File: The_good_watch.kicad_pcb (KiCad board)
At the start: 2 copper layers, 45 x 45 mm, 42 parts, among them IC1 DW01A, J1 Main, J2 USB_B_Micro, J3 PROG, J4 Screen, J5 Button, J6 70AAJ-6-M0G, M1 Motor_DC, Q1 FS8205A, SW1 SW_Push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

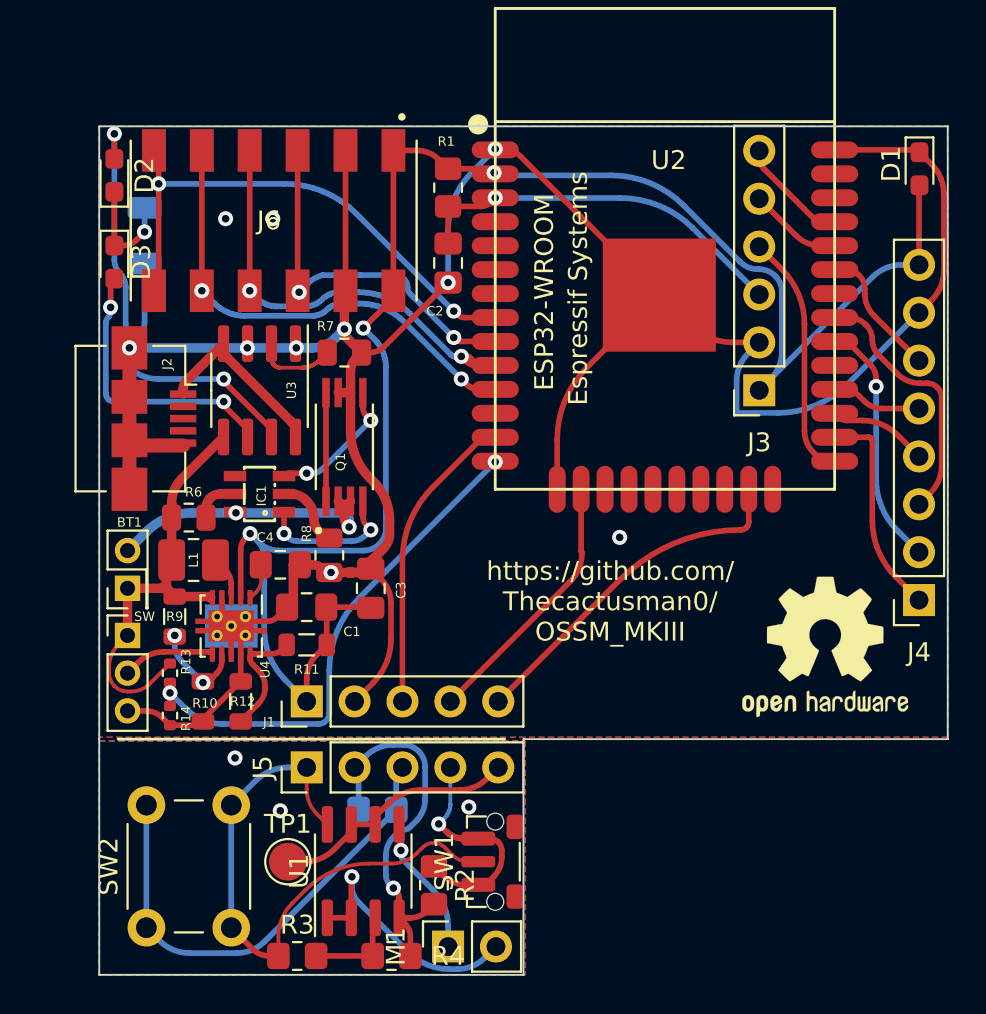
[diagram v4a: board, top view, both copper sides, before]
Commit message: Changed spring connector for modules to pinheaders.
still need to update modules
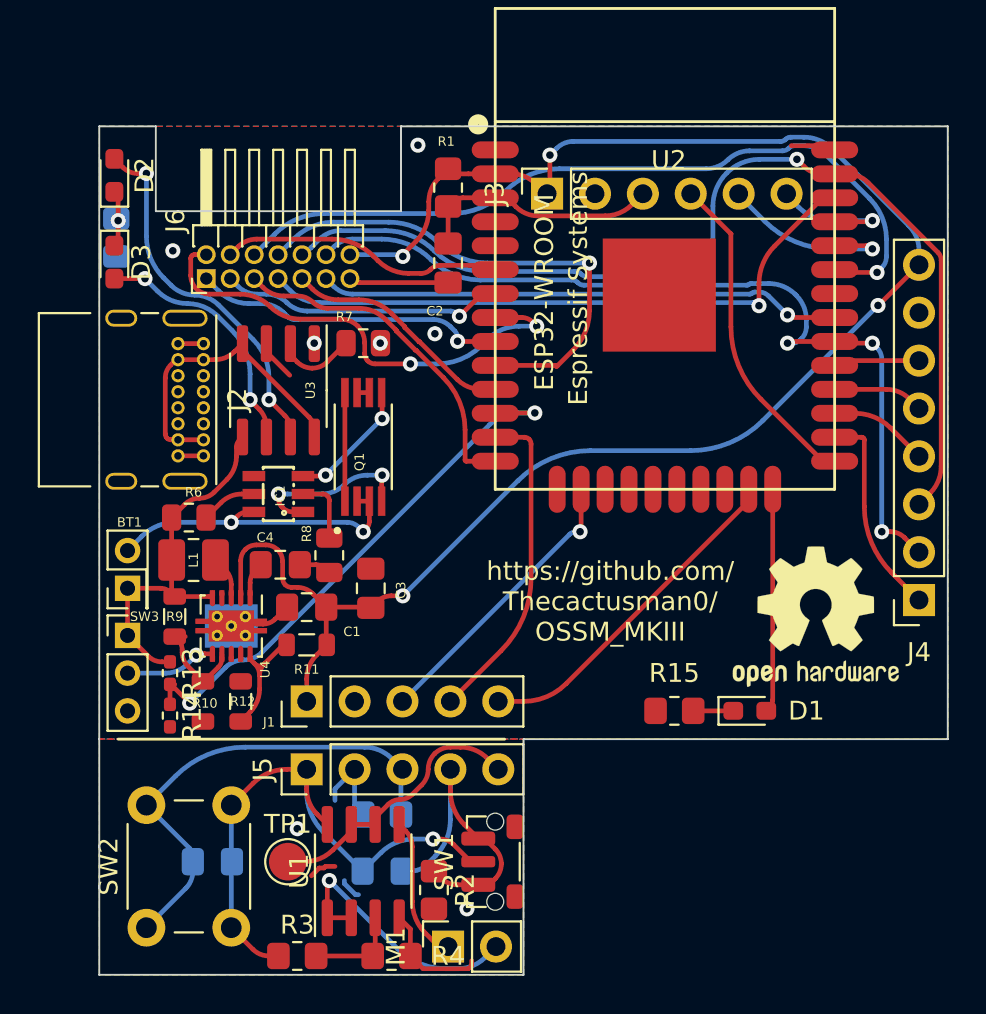
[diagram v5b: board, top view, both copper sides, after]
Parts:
- removed JP1: CHRG, Capacitor_SMD:C_1206_3216Metric
- added C5: 100nF, Capacitor_SMD:C_0805_2012Metric_Pad1.18x1.45mm_HandSolder, B.Cu at (115.0, 89.5)
- added C6: 100nF, Capacitor_SMD:C_0805_2012Metric_Pad1.18x1.45mm_HandSolder, B.Cu at (106.0, 89.0)
- added R15: 2K, Resistor_SMD:R_0805_2012Metric_Pad1.20x1.40mm_HandSolder, F.Cu at (130.5, 81.0)
- added R16: 2K, Resistor_SMD:R_0805_2012Metric_Pad1.20x1.40mm_HandSolder, B.Cu at (100.9, 55.9)
- C2: value 0.1uF -> 1uF
- J2: value USB_B_Micro -> USB_C_Receptacle_USB2.0; footprint Connector_USB:USB_Micro-B_Amphenol_10104110_Horizontal -> Connector_USB:USB_C_Receptacle_GCT_USB4085
- J6: value 70AAJ-6-M0G -> Conn_02x07_Counter_Clockwise; footprint 70AAJ-6-M0G:BOURNS_70AAJ-6-M0G -> Connector_PinHeader_1.27mm:PinHeader_2x07_P1.27mm_Horizontal
- R13, R14: footprint Resistor_SMD:R_0402_1005Metric -> Resistor_SMD:R_0402_1005Metric_Pad0.72x0.64mm_HandSolder
- moved D1 30.1 mm to (134.5, 81.0), turned to 0 degrees
- moved J3 15.3 mm to (123.8, 53.6), turned to 90 degrees
- moved J2 4.76 mm to (105.5, 61.5)
- moved J6 4.72 mm to (105.7, 58.1), turned to 90 degrees
- moved REF** 1.68 mm to (138.0, 76.0)
- moved R7 1.12 mm to (114.0, 61.5)
- moved IC1 1.00 mm to (109.5, 69.5)
- moved Q1 1.00 mm to (114.0, 67.0)
- moved U3 1.00 mm to (109.5, 64.0)
- moved R5 0.35 mm to (115.0, 86.5)
- moved R2 0.25 mm to (117.8, 90.5)
- moved J5 0.10 mm to (111.0, 84.1)
- renumbered SW to SW3
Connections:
- D1 pad 1: GND -> Net-(D1-Pad1)
- D1 pad 2: +3V3 -> IO2
- J6 pad 1: +3V3 -> SENSE
- J6 pad 10: SENSE -> MOSI
- J6 pad 11: GND -> MISO
- J6 pad 12: +3V3 -> SCK
- J6 pad 2: GND -> ANALOG0
- J6 pad 3: SENSE -> ANALOG1
- J6 pad 4: SDA -> ANALOG2
- J6 pad 5: SCL -> MGPIO0
- J6 pad 6: ANALOG -> MGPIO1
- J6 pad 7: ANALOG -> MGPIO2
- J6 pad 8: SCL -> SDA
- J6 pad 9: SDA -> SCL
- Q1 pad 1: Net-(Q1-Pad1) -> unconnected-(Q1-Pad1)
- Q1 pad 8: Net-(Q1-Pad1) -> unconnected-(Q1-Pad1)
- R13 pad 2: IO12 -> IO27
- R14 pad 1: IO12 -> IO27
- U2 pad 12: unconnected-(U2-Pad12) -> IO27
- U2 pad 13: B2_M -> B1_M
- U2 pad 14: IO12 -> MGPIO0
- U2 pad 16: B1_M -> B2_M
- U2 pad 24: unconnected-(U2-Pad24) -> IO2
- U2 pad 29: unconnected-(U2-Pad29) -> CS
- U2 pad 31: MOSI -> MISO
- U2 pad 33: CS -> MGPIO1
- U2 pad 36: MISO -> MGPIO2
- U2 pad 37: unconnected-(U2-Pad37) -> MOSI
- U2 pad 6: unconnected-(U2-Pad6) -> ANALOG2
- U2 pad 7: unconnected-(U2-Pad7) -> ANALOG1
- U2 pad 8: ANALOG -> ANALOG0
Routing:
- net GND: track 180.7 -> 27.6 mm, vias 14 -> 7
- net MGPIO1: track 0.00 -> 42.0 mm, vias 0 -> 1
- net MOSI: track 13.9 -> 55.2 mm, vias 0 -> 1
- net MGPIO2: track 0.00 -> 33.6 mm, vias 0 -> 1
- net SCK: track 13.1 -> 46.4 mm, vias 1 -> 3
- net IO27: track 0.00 -> 29.3 mm, vias 0 -> 2
- net ANALOG: track 28.2 -> 0.00 mm, vias 2 -> 0
- net MISO: track 0.00 -> 27.8 mm, vias 0 -> 1
- net IO12: track 27.2 -> 0.00 mm, vias 2 -> 0
- net ANALOG0: track 0.00 -> 27.1 mm, vias 0 -> 2
- net MGPIO0: track 0.00 -> 18.2 mm
- net ANALOG1: track 0.00 -> 15.1 mm, vias 0 -> 1
- net ANALOG2: track 0.00 -> 15.0 mm
- net SCL: track 25.3 -> 12.4 mm, vias 2 -> 0
- net IO2: track 0.00 -> 11.9 mm
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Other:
- outline, holes or cut-outs redrawn

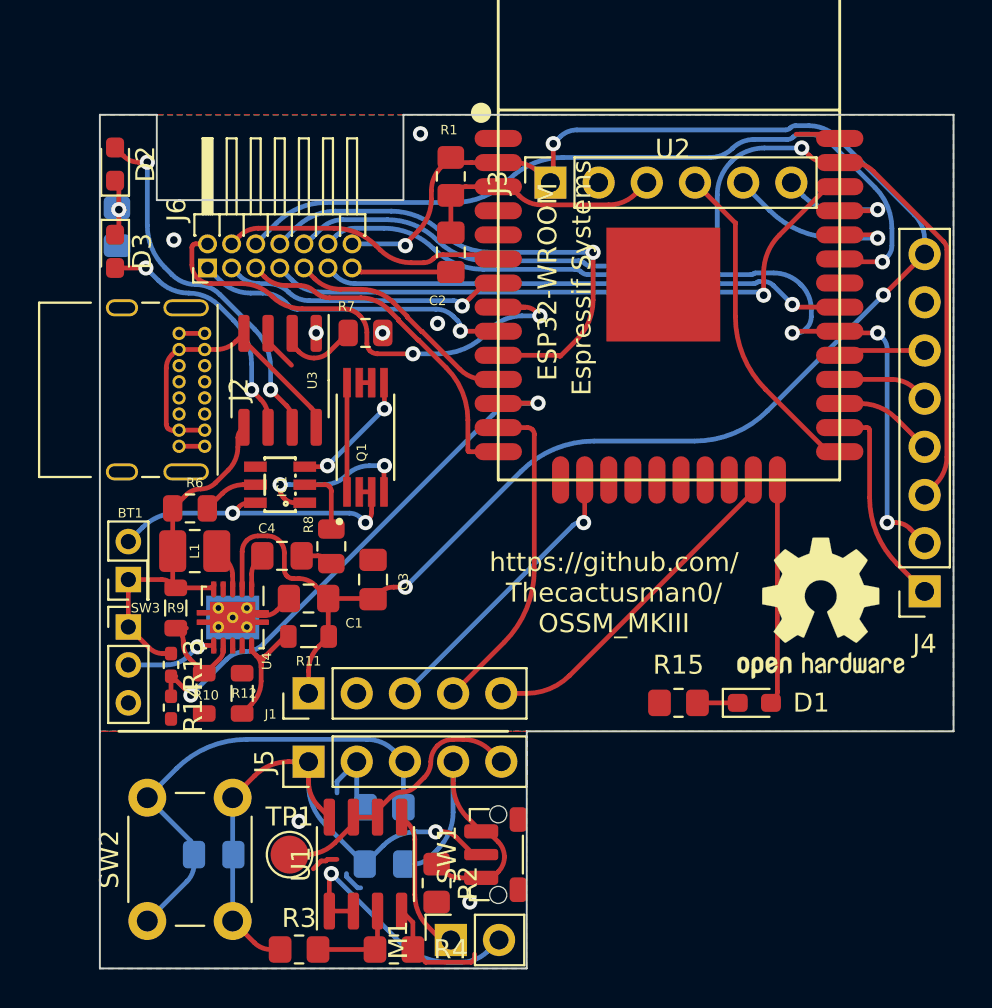
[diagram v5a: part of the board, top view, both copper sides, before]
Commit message: Graphical fixes, minor electrical fixes and enviro sensor module trial
Fixed some component values and added i2c pullups
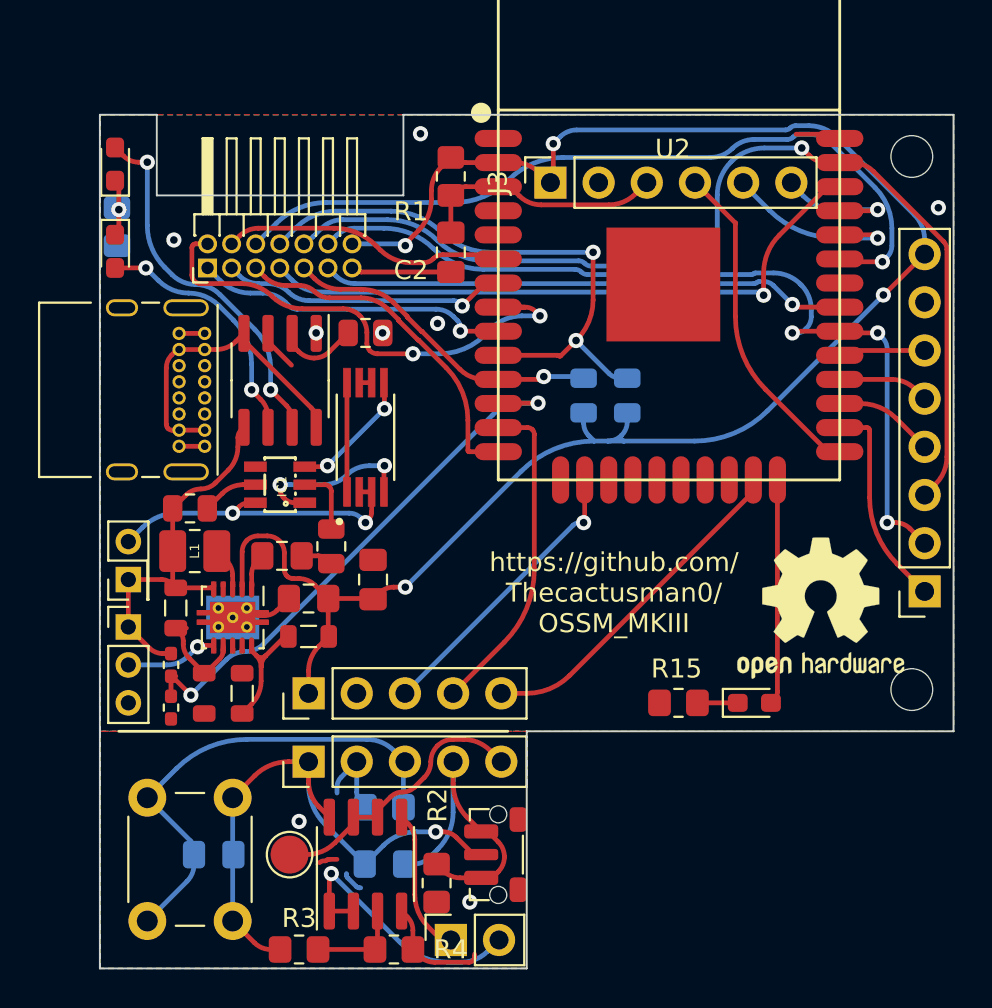
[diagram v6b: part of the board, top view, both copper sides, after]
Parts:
- added R17: 4.7K, Resistor_SMD:R_0805_2012Metric, B.Cu at (125.5, 64.8)
- added R18: 4.7K, Resistor_SMD:R_0805_2012Metric, B.Cu at (127.8, 64.8)
- added REF**: MountingHole_2.2mm_M2, MountingHole:MountingHole_2.2mm_M2, F.Cu at (142.8, 52.2)
- added REF**: MountingHole_2.2mm_M2, MountingHole:MountingHole_2.2mm_M2, F.Cu at (142.8, 80.3)
- renumbered Q1 to Qe, R8 to Re
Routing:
- net SCL: track 12.4 -> 17.0 mm, vias 0 -> 1
- net +3V3: track 123.2 -> 127.3 mm
- net SDA: track 27.0 -> 30.4 mm, vias 1 -> 2
- net (no net): track 2.61 -> 0.00 mm
- net GND: track 27.6 -> 29.4 mm, vias 7 -> 8
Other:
- outline, holes or cut-outs redrawn

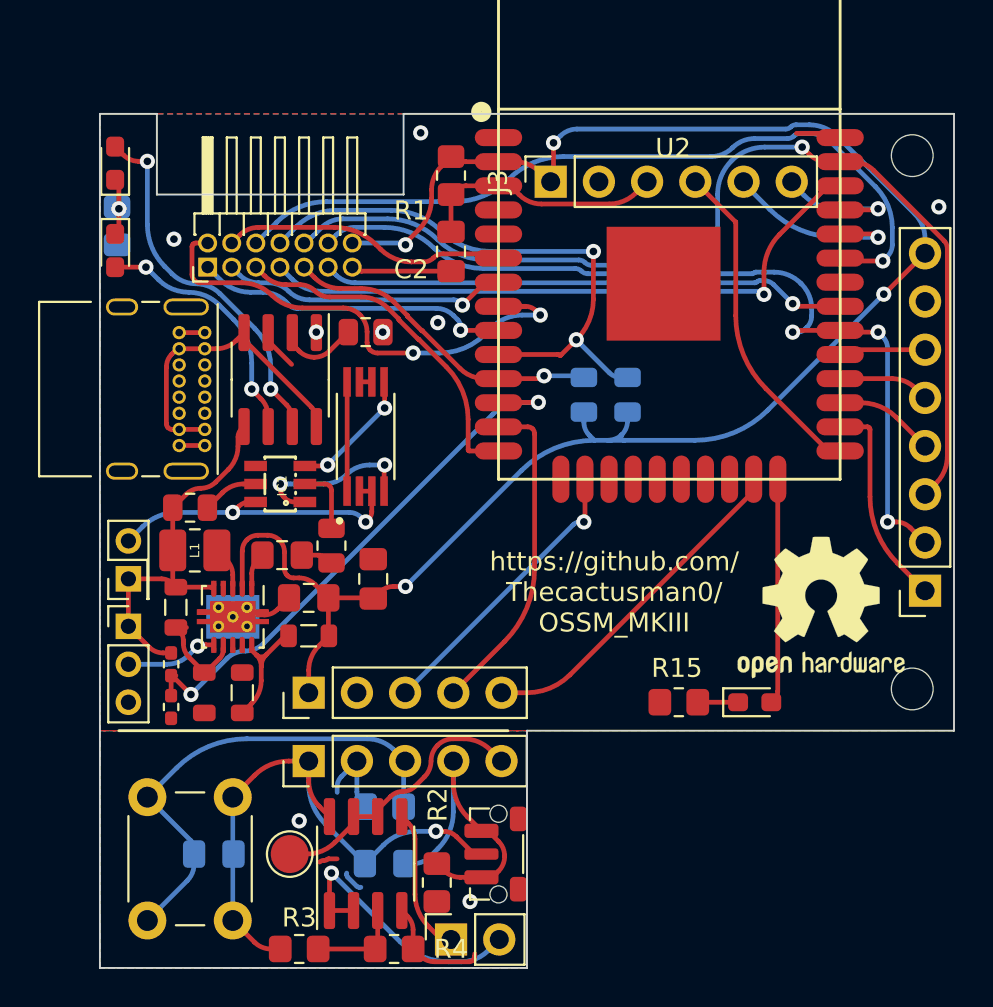
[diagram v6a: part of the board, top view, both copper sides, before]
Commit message: Added power switching
Uses usb power when plugged in and disconnects battery.
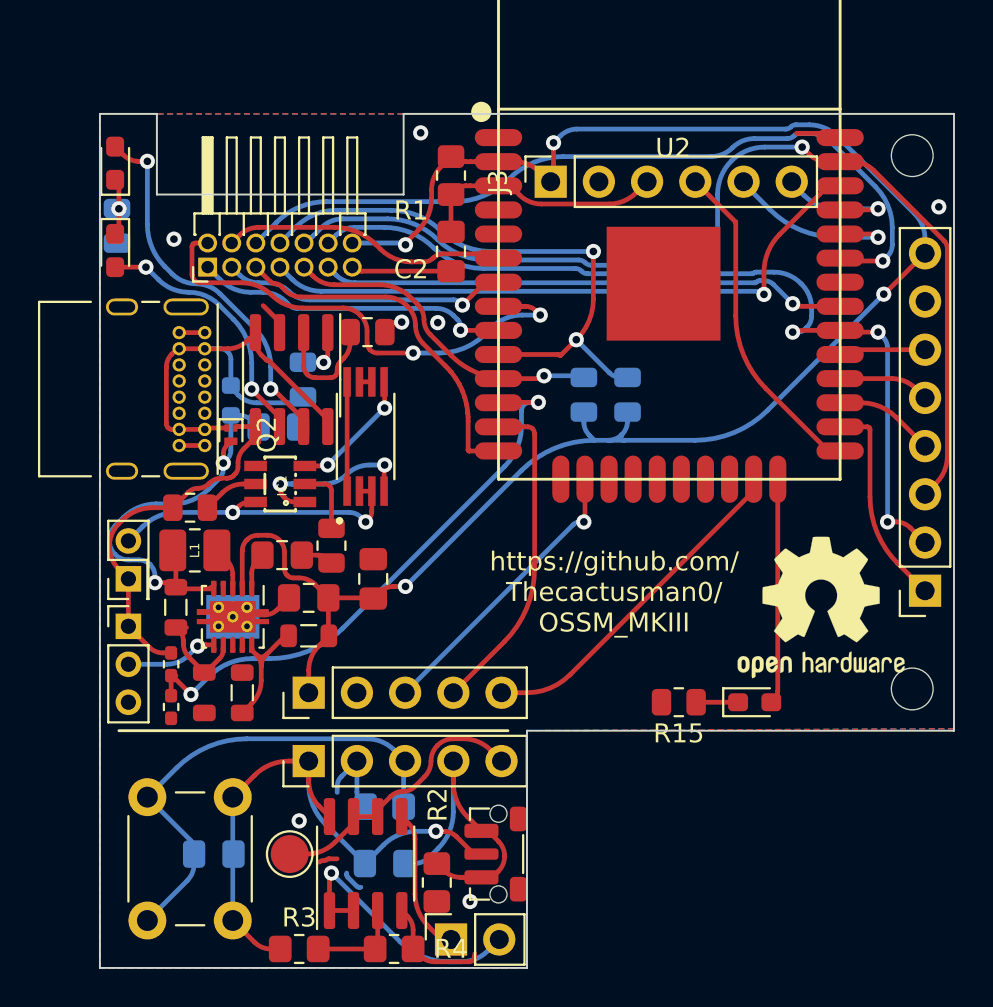
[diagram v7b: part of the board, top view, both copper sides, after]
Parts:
- added C7: 1uF, Capacitor_SMD:C_0805_2012Metric_Pad1.18x1.45mm_HandSolder, B.Cu at (109.4, 66.5)
- added D4: D_Schottky, Diode_SMD:D_0603_1608Metric, B.Cu at (106.9, 65.1)
- added Q2: LP0404N3T5G, Package_TO_SOT_SMD:SOT-883, F.Cu at (106.9, 66.9)
- added R19: 100K, Resistor_SMD:R_0805_2012Metric, B.Cu at (110.7, 64.0)
- R15, R16: footprint Resistor_SMD:R_0805_2012Metric_Pad1.20x1.40mm_HandSolder -> Resistor_SMD:R_0805_2012Metric
- moved U3 0.60 mm to (110.1, 64.0)
- moved R7 0.10 mm to (114.1, 61.5)
- renumbered Qe to Q1, Re to R8
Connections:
- L1 pad 1: +BATT -> PSU
- R9 pad 1: +BATT -> PSU
- U4 pad 5: +BATT -> PSU
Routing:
- net PSU: track 0.00 -> 22.8 mm, vias 0 -> 2
- net VCC_IN: track 16.4 -> 25.3 mm
- net Net-(R7-Pad1): track 4.25 -> 6.32 mm
- net GND: track 29.4 -> 31.2 mm
- net IO27: track 29.3 -> 30.2 mm
- net +BATT: track 20.4 -> 19.7 mm
- net MGPIO0: track 18.2 -> 18.9 mm

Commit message: Fixed connector problems
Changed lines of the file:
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@@
   (arc (start 108 64.512307) (mid 108.002261 64.523677) (end 108.008702 64.533316) (width 0.25) (layer "F.Cu") (net 15))
   (arc (start 109.29339 65.818004) (mid 109.4204 66.008087) (end 109.465 66.232307) (width 0.25) (layer "F.Cu") (net 15))
-  (segment (start 107.039983 60.824647) (end 106.275311 60.059975) (width 0.25) (layer "B.Cu") (net 15))
+  (segment (start 107.039983 60.824647) (end 105.792884 59.577548) (width 0.25) (layer "B.Cu") (net 15))
   (segment (start 108 63.142332) (end 108 64.5) (width 0.25) (layer "B.Cu") (net 15))
+  (segment (start 104.683148 59.40048) (end 105.365453 59.400495) (width 0.25) (layer "B.Cu") (net 15))
   (segment (start 102.425 58.075) (end 103.090984 58.740984) (width 0.25) (layer "B.Cu") (net 15))
-  (arc (start 104.683148 59.40048) (mid 105.54482 59.571877) (end 106.275311 60.059975) (width 0.25) (layer "B.Cu") (net 15))
+  (arc (start 105.365453 59.400495) (mid 105.596777 59.446512) (end 105.792884 59.577548) (width 0.25) (layer "B.Cu") (net 15))
   (arc (start 103.090984 58.740984) (mid 103.821475 59.229082) (end 104.683148 59.40048) (width 0.25) (layer "B.Cu") (net 15))
   (arc (start 108 63.142332) (mid 107.750499 61.88801) (end 107.039983 60.824647) (width 0.25) (layer "B.Cu") (net 15))
